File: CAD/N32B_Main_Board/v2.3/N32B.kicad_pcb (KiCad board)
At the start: 2 copper layers, 200 x 130 mm, 61 parts, among them IC1 MAX7219CNG, J1 AudioJack4, J2 AudioJack4, U1 6N138

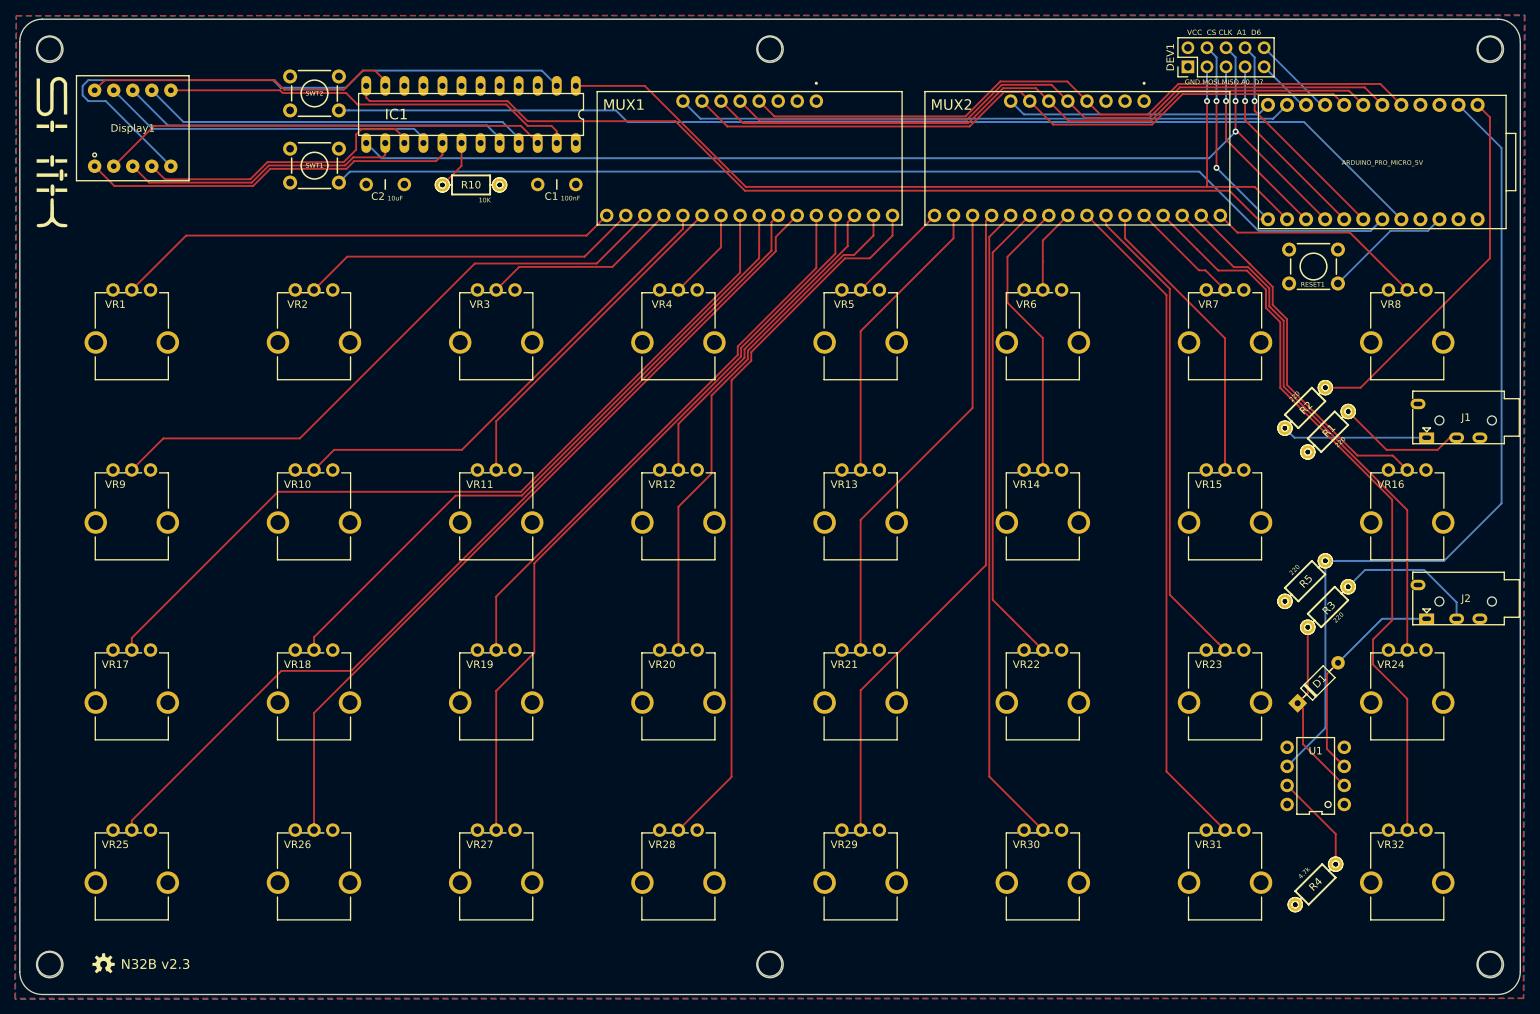
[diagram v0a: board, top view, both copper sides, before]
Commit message: Adding enclosure files. Cleanup.
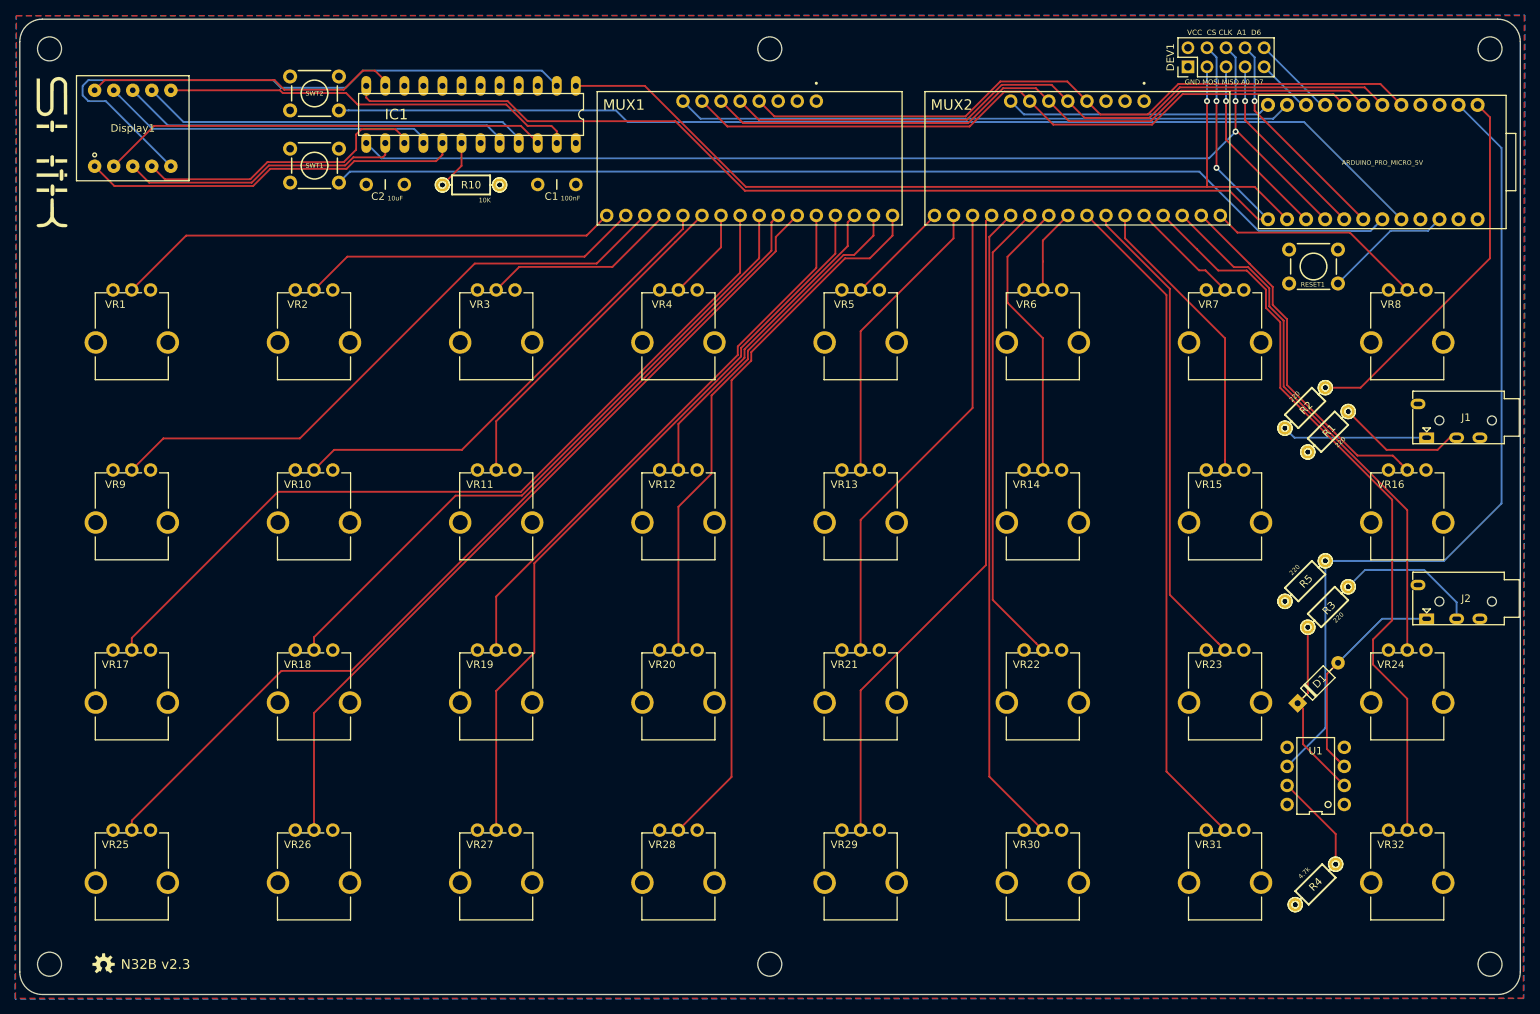
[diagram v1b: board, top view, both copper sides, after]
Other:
- outline, holes or cut-outs redrawn
- net class Default removed
